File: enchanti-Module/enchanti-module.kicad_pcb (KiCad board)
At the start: 4 copper layers, 46 x 46 mm, 77 parts, among them J2 Programming Header, J5 CONN_MEZANNINE, U1 Sona-IF573, U10 ICM-42670-P, U12 MMC5633NJL, U13 B3U-1000P, U2 STM32H7R3V8T6, U3 NCP167AMX180TBG, U4 B3U-1000P, U6 NCP187AMT330TAG, U8 S76HS512TC0BHB010, U9 TCAN3413DRBR

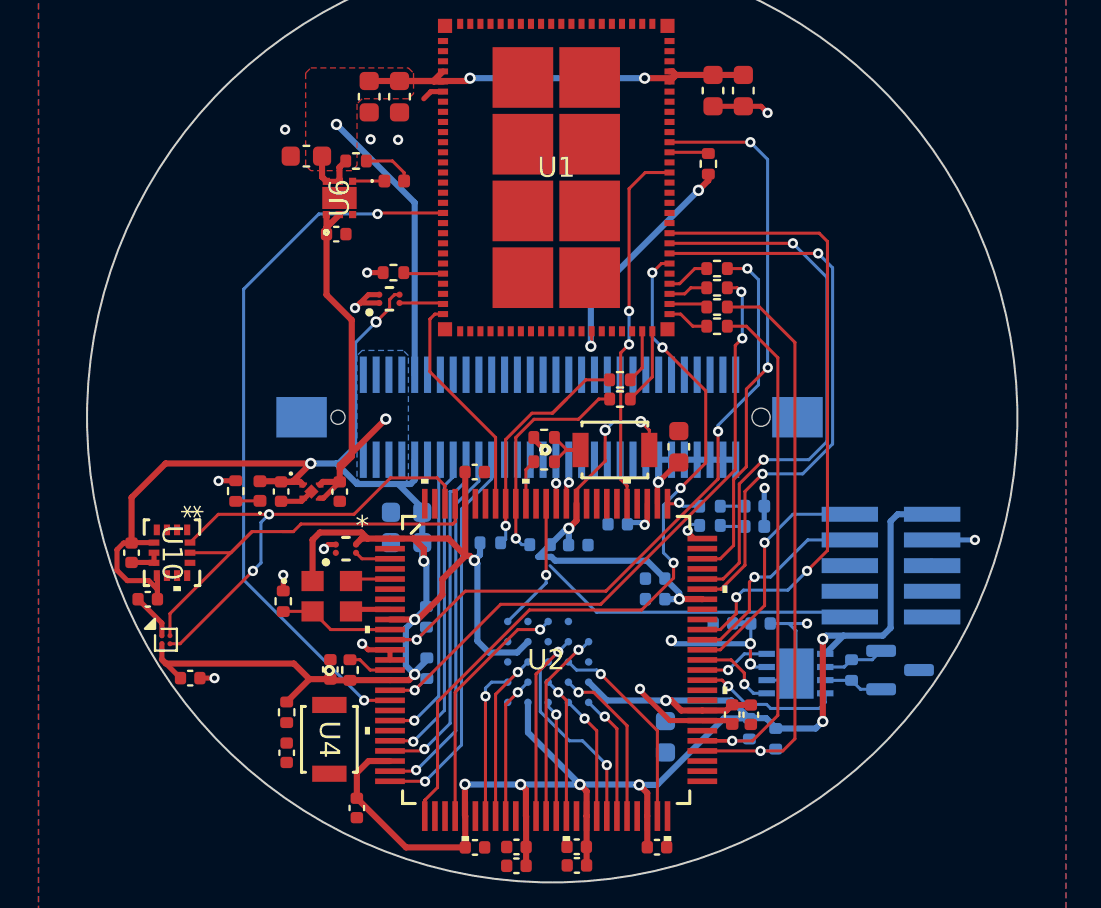
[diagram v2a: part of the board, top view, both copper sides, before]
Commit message: added back USB connector, added power path manager, went with smaller connector
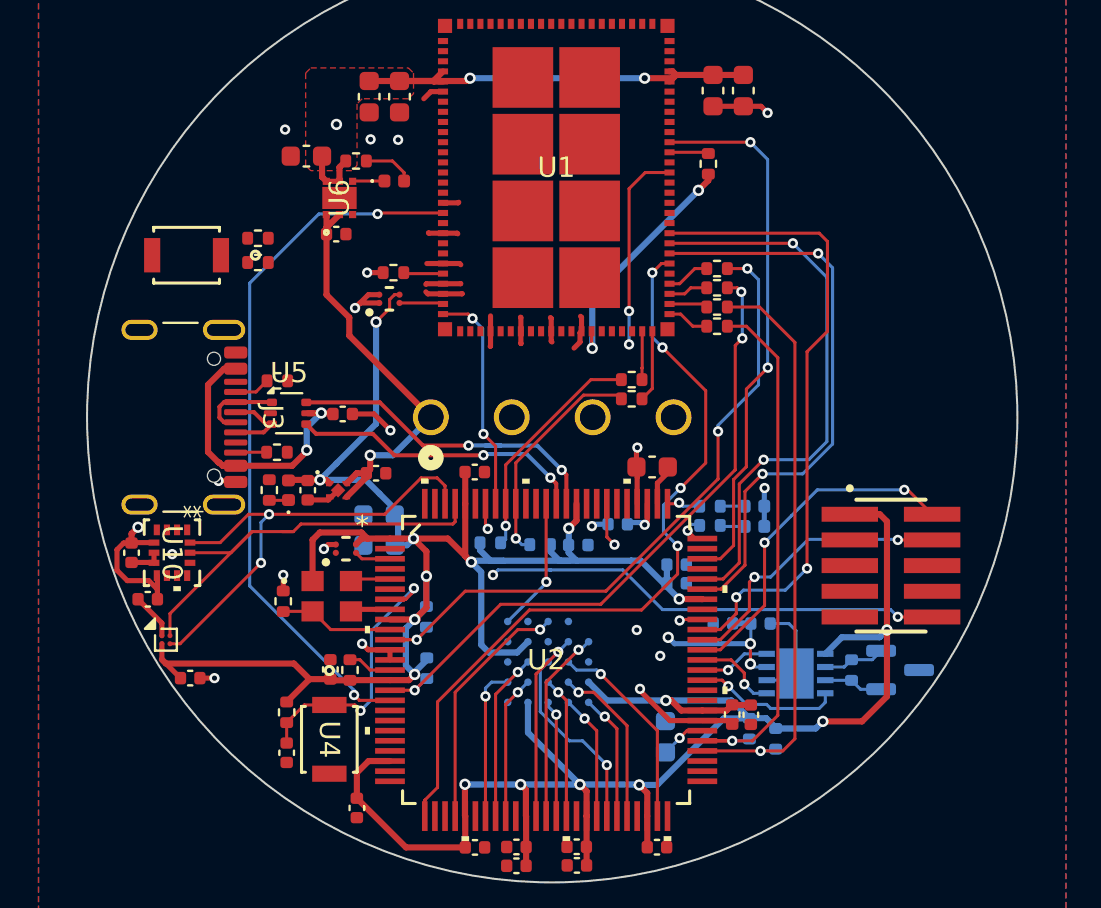
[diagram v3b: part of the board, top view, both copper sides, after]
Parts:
- removed J5: CONN_MEZANNINE, ENCHANTI_connectors:CON_536250674_MOL
- added C23: 0.1uF, Capacitor_SMD:C_0402_1005Metric, F.Cu at (82.3, 76.0)
- added J1: 878-22-004-10-011101, ENCHANTI_connectors:CONN_878-22-004-10-011101_MIM, B.Cu at (86.7, 76.2)
- added J3: USB_C_Receptacle_USB2.0, Connector_USB:USB_C_Receptacle_GCT_USB4105-xx-A_16P_TopMnt_Horizontal, F.Cu at (73.4, 76.2)
- added R24: 5k1, Resistor_SMD:R_0402_1005Metric, F.Cu at (79.1, 77.9)
- added R26: 5k1, Resistor_SMD:R_0402_1005Metric, F.Cu at (79.1, 74.4)
- added U5: USBLC6-2P6, Package_TO_SOT_SMD:SOT-666, F.Cu at (79.7, 76.0)
- J2: moved to F.Cu
- moved U13 23.3 mm to (74.6, 68.2), turned to 180 degrees
- moved R8 18.0 mm to (78.2, 67.3), turned to 180 degrees
- moved R14 16.6 mm to (78.2, 68.5), turned to 180 degrees
- moved C4 2.01 mm to (84.0, 79.0), turned to 0 degrees
- moved C14 2.01 mm to (98.9, 83.5), turned to 0 degrees
- moved R10 1.66 mm to (78.7, 79.8)
- moved C27 1.66 mm to (97.7, 78.7), turned to 180 degrees
- moved PGLED2 1.41 mm to (79.7, 79.8)
- moved C15 1.37 mm to (84.2, 82.5)
- moved C8 1.37 mm to (84.2, 81.0)
- moved C6 1.32 mm to (80.6, 79.8)
- moved U3 1.32 mm to (82.1, 79.8)
- moved C16 1.08 mm to (98.9, 84.4), turned to 0 degrees
- moved R12 0.58 mm to (96.6, 75.3)
- moved R7 0.58 mm to (96.6, 74.3)
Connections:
- U2 pad 100: /BTN2 -> unconnected-(U2A-PB9-Pad100)
- U2 pad 2: /LED1 -> unconnected-(U2A-PC13-Pad2)
- U2 pad 27: /ANG2 -> unconnected-(U2A-PB1-Pad27)
- U2 pad 28: /ANG3 -> unconnected-(U2A-PB2-Pad28)
- U2 pad 60: /LED2 -> unconnected-(U2A-PA9-Pad60)
- U2 pad 81: /FSR2 -> unconnected-(U2A-PM6-Pad81)
- U2 pad 83: /FSR1 -> unconnected-(U2A-PM8-Pad83)
- U2 pad 99: /BTN1 -> unconnected-(U2A-PB8-Pad99)
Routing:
- net /VCAP: track 0.00 -> 31.2 mm, vias 0 -> 4
- net /NRST: track 15.7 -> 40.8 mm, vias 0 -> 4
- net /I2S6_SDO/SPI1_MOSI: track 19.0 -> 0.00 mm, vias 1 -> 0
- net /I2S6_SDI/SPI1_MISO: track 18.0 -> 0.00 mm, vias 1 -> 0
- net /I2S6_CK/SPI1_SCK: track 17.1 -> 0.00 mm, vias 1 -> 0
- net /I2S6_WS/SPI1_NSS: track 15.9 -> 0.00 mm, vias 1 -> 0
- net /I2S6_MCK: track 14.6 -> 0.00 mm, vias 1 -> 0
- net GND: track 38.4 -> 52.9 mm, vias 16 -> 19
- net /USBD-: track 2.23 -> 16.6 mm, vias 1 -> 2
- net +1V8: track 214.5 -> 201.9 mm
- net /USBD+: track 2.18 -> 14.6 mm, vias 1 -> 2
- net +3V3: track 80.2 -> 68.0 mm
- net /BT_REG_ON: track 18.2 -> 10.0 mm
- net VUSB: track 8.06 -> 16.1 mm, vias 1 -> 2
- net /SWDIO: track 11.9 -> 17.0 mm, vias 1 -> 2
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- removed copper zone on B.Cu, net SYS
